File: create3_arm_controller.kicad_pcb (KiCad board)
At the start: 2 copper layers, 126.4 x 103.7 mm, 233 parts, among them IC1 TPS40192DRCT-TPS40192DRCT, IC2 TPS40192DRCT-TPS40192DRCT, IC3 LMR14010A, J1 USB_C_Receptacle, J10 Conn_01x03_Female, J11 Conn_01x03_Female, J12 Conn_01x03_Female, J13 Conn_01x03_Female, J14 Conn_01x03_Female, J15 USB_C_Receptacle, J16 USB_C_Receptacle, J17 USB3_A, J18 USB3_A, J19 Conn_01x06_Female, J2 Conn_ARM_JTAG_SWD_10, J20 Conn_01x04_Female, J21 Conn_01x04_Female, J22 Conn_01x04_Female, J23 Conn_01x04_Female, J24 Conn_01x04_Female, J25 Conn_01x04_Female, J26 Micro_SD_Card_Det, J27 Conn_01x22_Female, J28 Conn_01x22_Female, J29 690-019-298-412, J3 Conn_01x03_Female, J30 Conn_01x02_Female, J32 Molex 470531000, J33 USB_OTG, J34 690-008-221-904, J4 Conn_01x03_Female, J5 Conn_01x03_Female, J6 Conn_01x03_Female, J7 Conn_01x03_Female, J8 Conn_01x03_Female, J9 Conn_01x03_Female, Q1 BUK9M17-30EX / BUK7M10-40E, Q2 BUK9M17-30EX / BUK7M10-40E, Q3 BUK9M17-30EX / BUK7M10-40E, Q4 BUK9M17-30EX / BUK7M10-40E, Q5 DMP3013SFV-7, SW1 SW_DIP_x01, U1 TLV71211_SOT23-5, U10 TPD4EUSB30, U11 TPS2560, U12 TPS2560, U13 74LVC1G07SE-7, U14 74LVC1G07SE-7, U15 RT9742GGJ5, U16 RT9742SNGV, U17 AP64501SP-13, U18 PCF85063AT/AAZ, U19 EMC2301-1-ACZL-TR, U2 74LS125, U20 74LVC1G07SE-7, U21 FSUSB42MUX, U22 USB2514B-I/M2, U23 TPD4EUSB30, U24 AP22653W6, U3 STM32F303VETx, U4 TPD4EUSB30, U5 TPD4EUSB30, U6 TUSB7340, U7 TPD4EUSB30, U8 TPD4EUSB30, U9 TPD4EUSB30, Y1 Crystal_Small, Y2 Crystal_Small, Y3 Crystal_Small, Y4 X32K768S301, Y5 24MHz

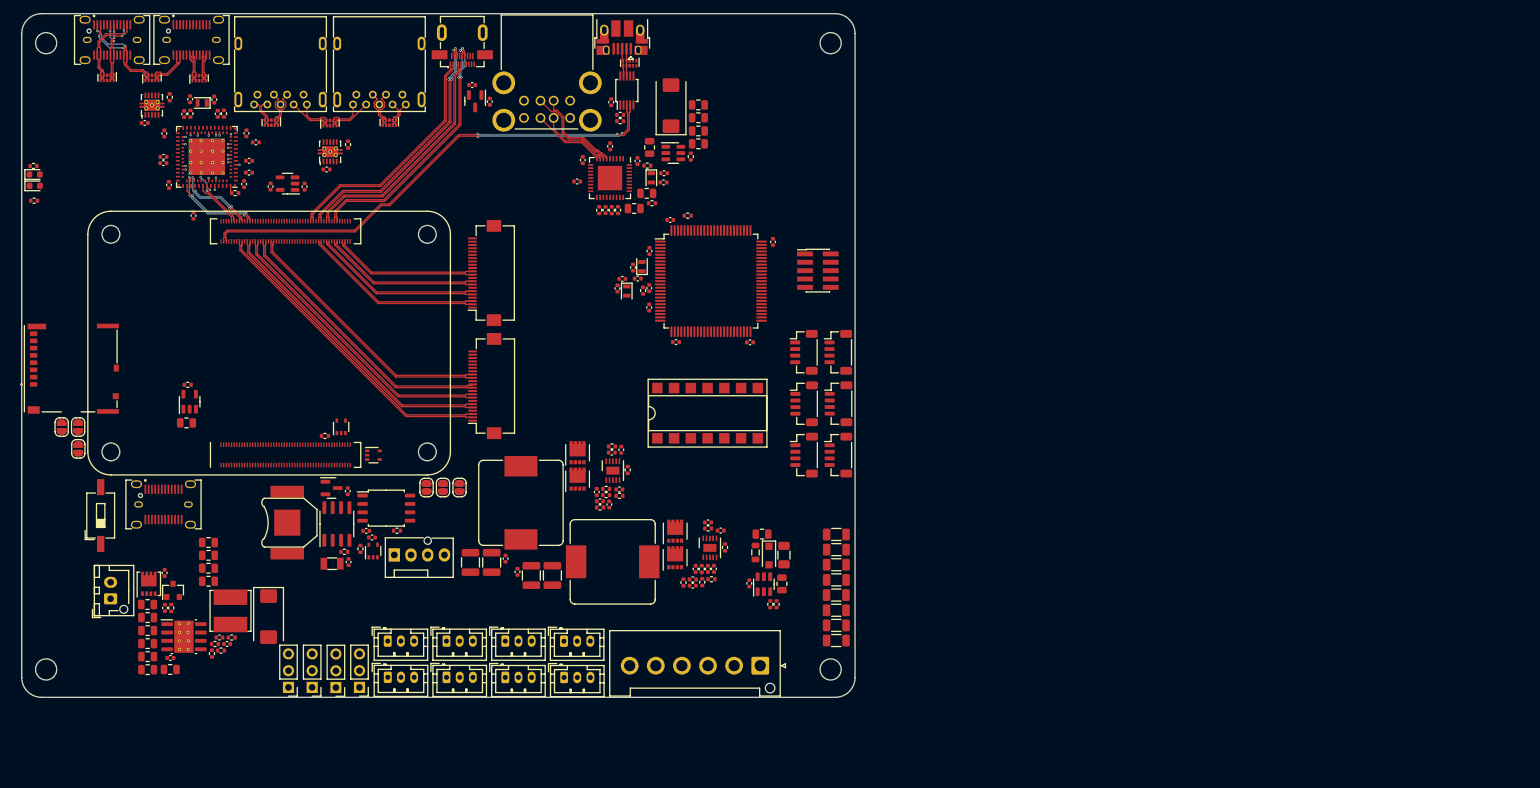
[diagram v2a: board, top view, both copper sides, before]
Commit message: mostly routed, need to add more layers fo power and finish low speed signal routing
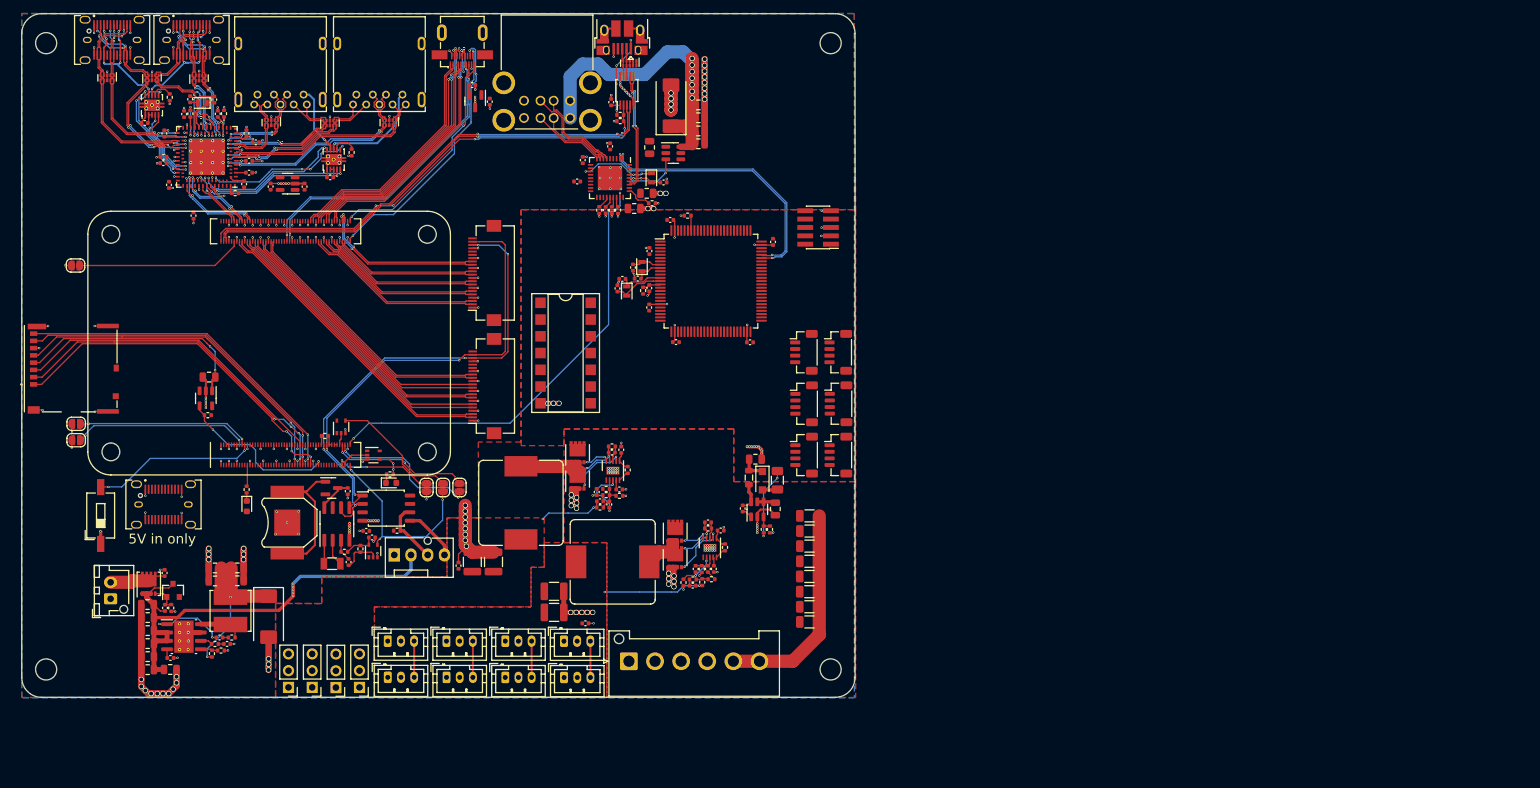
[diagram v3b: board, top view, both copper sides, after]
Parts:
- removed C83: 27pF, Capacitor_SMD:C_0402_1005Metric
- removed C92: 100nF, Capacitor_SMD:C_0402_1005Metric
- removed R43: 12K 1%, Resistor_SMD:R_0402_1005Metric
- removed R45: 15K 1%, Resistor_SMD:R_0402_1005Metric
- moved D5 71.5 mm to (89.0, 97.7)
- moved R28 71.5 mm to (88.9, 96.4)
- moved D4 58.3 mm to (67.1, 101.2), turned to -90 degrees
- moved R26 54.4 mm to (67.1, 98.7), turned to 90 degrees
- moved JP5 24.5 mm to (41.2, 64.7), turned to 180 degrees
- moved U2 23.4 mm to (115.5, 78.0), turned to 0 degrees
- moved J19 19.9 mm to (125.1, 124.8), turned to 0 degrees
- moved C28 12.9 mm to (118.5, 119.0), turned to 0 degrees
- moved C56 11.4 mm to (142.4, 101.6)
- moved C57 11.4 mm to (147.3, 101.7)
- moved C58 11.4 mm to (144.3, 94.1)
- moved D3 11.4 mm to (145.3, 97.4)
- moved F1 11.4 mm to (147.6, 97.3)
- moved IC3 11.4 mm to (144.6, 101.7)
- moved L3 11.4 mm to (143.3, 96.9)
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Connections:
- J1 pad A4: /CM4IOv5/+5V -> /CM4IOv5/+5v
- J1 pad A9: /CM4IOv5/+5V -> /CM4IOv5/+5v
- J1 pad B4: /CM4IOv5/+5V -> /CM4IOv5/+5v
- J1 pad B9: /CM4IOv5/+5V -> /CM4IOv5/+5v
- J19 pad 5: /SUPPLIMENTARY_BATTERY/GND -> GND
- J19 pad 6: /SUPPLIMENTARY_BATTERY/GND -> GND
- U12 pad 8: /CM4IOv5/USB3/USB3_CONN/P2_VBUS -> /CM4IOv5/USB3/USB3_CONN/P1_VBUS
- U12 pad 9: /CM4IOv5/USB3/USB3_CONN/P1_VBUS -> /CM4IOv5/USB3/USB3_CONN/P2_VBUS
- U6 pad A10: /CM4IOv5/USB3/P2_RX_N -> /CM4IOv5/USB3/P4_RX_N
- U6 pad A11: /CM4IOv5/USB3/P2_TX_P -> /CM4IOv5/USB3/P4_TX_P
- U6 pad A13: /CM4IOv5/USB3/P2_DN -> /CM4IOv5/USB3/P4_DN
- U6 pad A17: /CM4IOv5/USB3/P1_TX_P -> /CM4IOv5/USB3/P2_TX_P
- U6 pad A18: /CM4IOv5/USB3/P1_RX_P -> /CM4IOv5/USB3/P2_RX_P
- U6 pad A20: /CM4IOv5/USB3/P1_DP -> /CM4IOv5/USB3/P2_DP
- U6 pad A27: /CM4IOv5/USB3/P3_DN -> /CM4IOv5/USB3/P1_DN
- U6 pad A29: /CM4IOv5/USB3/P3_RX_N -> /CM4IOv5/USB3/P1_RX_N
- U6 pad A30: /CM4IOv5/USB3/P3_TX_N -> /CM4IOv5/USB3/P1_TX_N
- U6 pad A5: /CM4IOv5/USB3/P4_DN -> /CM4IOv5/USB3/P3_DN
- U6 pad A7: /CM4IOv5/USB3/P4_RX_N -> /CM4IOv5/USB3/P3_RX_N
- U6 pad A8: /CM4IOv5/USB3/P4_TX_N -> /CM4IOv5/USB3/P3_TX_N
- U6 pad B10: /CM4IOv5/USB3/P2_TX_N -> /CM4IOv5/USB3/P4_TX_N
- U6 pad B12: /CM4IOv5/USB3/P2_DP -> /CM4IOv5/USB3/P4_DP
- U6 pad B15: /CM4IOv5/USB3/P1_TX_N -> /CM4IOv5/USB3/P2_TX_N
- U6 pad B16: /CM4IOv5/USB3/P1_RX_N -> /CM4IOv5/USB3/P2_RX_N
- U6 pad B18: /CM4IOv5/USB3/P1_DN -> /CM4IOv5/USB3/P2_DN
- U6 pad B25: /CM4IOv5/USB3/P3_DP -> /CM4IOv5/USB3/P1_DP
- U6 pad B27: /CM4IOv5/USB3/P3_RX_P -> /CM4IOv5/USB3/P1_RX_P
- U6 pad B28: /CM4IOv5/USB3/P3_TX_P -> /CM4IOv5/USB3/P1_TX_P
- U6 pad B5: /CM4IOv5/USB3/P4_DP -> /CM4IOv5/USB3/P3_DP
- U6 pad B6: /CM4IOv5/USB3/P4_RX_P -> /CM4IOv5/USB3/P3_RX_P
- U6 pad B7: /CM4IOv5/USB3/P4_TX_P -> /CM4IOv5/USB3/P3_TX_P
- U6 pad B9: /CM4IOv5/USB3/P2_RX_P -> /CM4IOv5/USB3/P4_RX_P
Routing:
- net GND: track 0.00 -> 316.4 mm, vias 0 -> 315
- net /CM4IOv5/CM4_HighSpeed/SCL0: track 0.00 -> 74.3 mm, vias 0 -> 5
- net /CM4IOv5/+12v: track 0.00 -> 73.7 mm, vias 0 -> 5
- net /CM4IOv5/CM4_HighSpeed/USBOTG_ID: track 0.00 -> 73.4 mm, vias 0 -> 4
- net /CM4IOv5/CM4_HighSpeed/SDA0: track 0.00 -> 70.7 mm, vias 0 -> 3
- net /CM4IOv5/nEXTRST: track 0.00 -> 68.9 mm, vias 0 -> 2
- net /CM4IOv5/USB2-HUB/VBUS: track 0.00 -> 60.2 mm, vias 0 -> 7
- net /CM4IOv5/CM4_GPIO ( Ethernet, GPIO, SDCARD)/SD_DAT2: track 0.00 -> 54.4 mm, vias 0 -> 3
- net /CM4IOv5/CM4_GPIO ( Ethernet, GPIO, SDCARD)/SD_DAT3: track 0.00 -> 53.2 mm, vias 0 -> 4
- net /CM4IOv5/CM4_GPIO ( Ethernet, GPIO, SDCARD)/SD_DAT1: track 0.00 -> 52.6 mm, vias 0 -> 2
- net /CM4IOv5/CM4_GPIO ( Ethernet, GPIO, SDCARD)/SD_DAT0: track 0.00 -> 52.3 mm, vias 0 -> 2
- net /CM4IOv5/CM4_GPIO ( Ethernet, GPIO, SDCARD)/SD_CLK: track 0.00 -> 52.3 mm, vias 0 -> 2
- net /CM4IOv5/CM4_GPIO ( Ethernet, GPIO, SDCARD)/SD_CMD: track 0.00 -> 49.1 mm
- net /CM4IOv5/CM4_HighSpeed/HDMI0_HOTPLUG: track 0.00 -> 45.3 mm, vias 0 -> 2
- net /CM4IOv5/CM4_HighSpeed/HDMI0_CEC: track 0.00 -> 45.3 mm, vias 0 -> 2
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- added copper zone on F.Cu, net +3V3
- added copper zone on F.Cu, net /CM4IOv5/+5v
- added copper zone on F.Cu, net /REGULATED_MOTOR_12V
- added copper zone on F.Cu, net /REGULATED_MOTOR_6V
- added copper zone on F.Cu, net /SUPPLIMENTAL_BATTERY
- added copper zone on B.Cu, net GND
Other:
- board text added: "5V in only"
